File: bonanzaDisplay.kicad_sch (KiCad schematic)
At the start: 73 parts, among them J1 OLED-1.31-SSD1322, J15 SWD, J5 Conn_01x10, J6 USB_C_Receptacle_USB2.0, SW1 TS-1088-AR02016, SW2 TS-1088-AR02016, SW4 7*7*5-6P WX, U1 RP2354A, U10 TPS82130, U2 XC6206P302MR, U3 XC6206P282MR, Y1 ABM8-272-T3

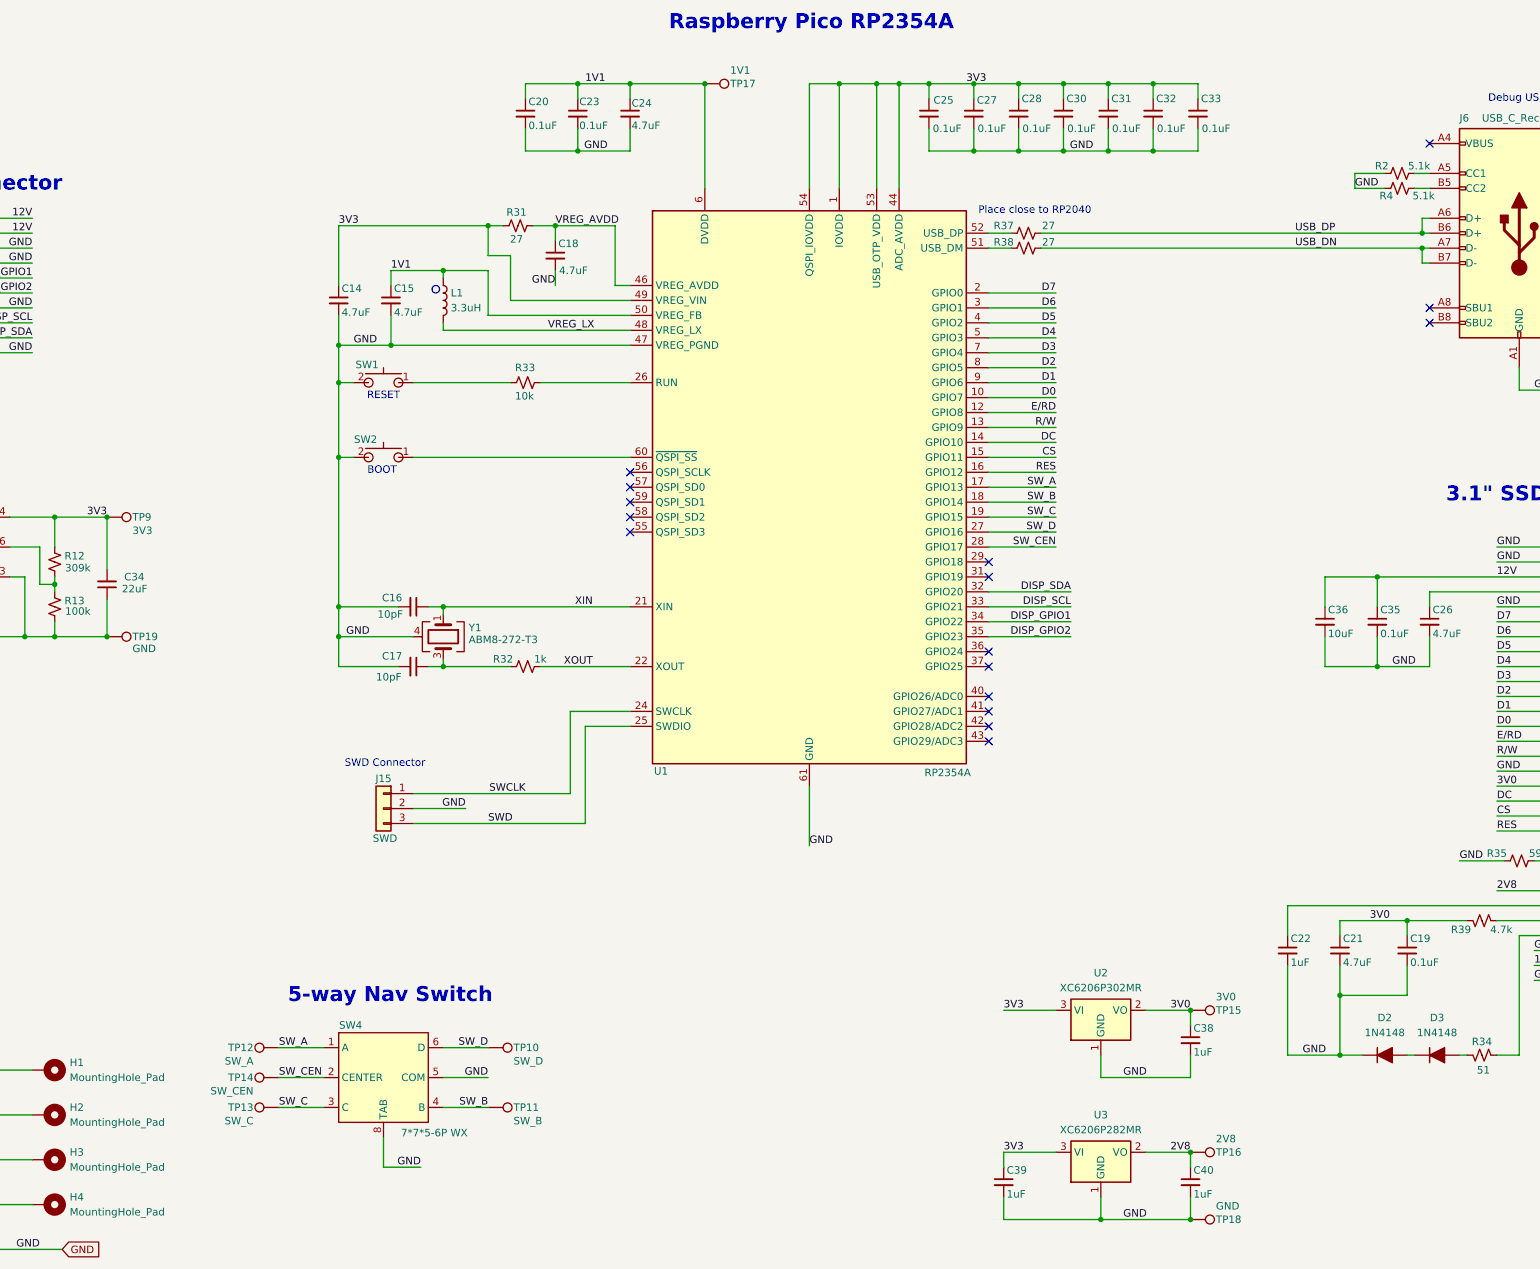
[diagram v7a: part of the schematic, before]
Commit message: updated LCSC part numbers
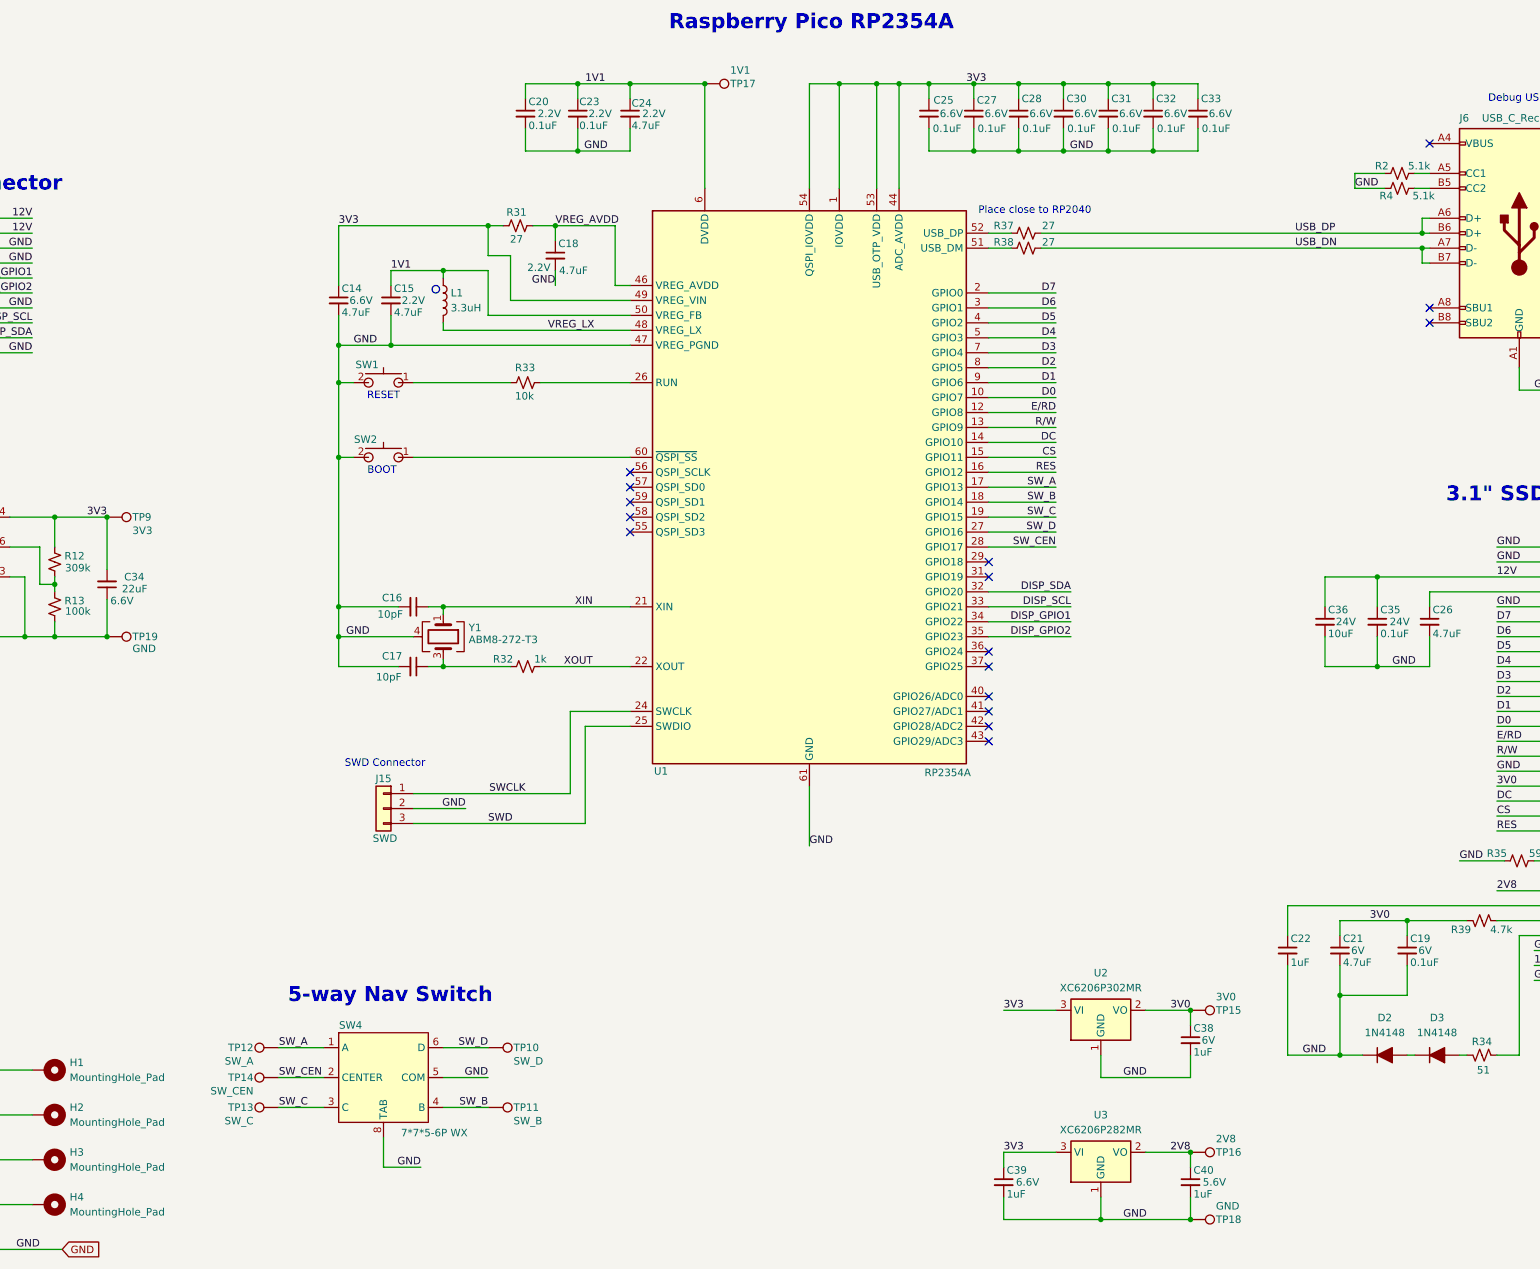
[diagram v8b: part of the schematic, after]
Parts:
- C14: LCSC (none) -> C368809; Voltage (none) -> 6.6V
- C15, C18, C24: LCSC (none) -> C368809; Voltage (none) -> 2.2V
- C16, C17: LCSC (none) -> C161512
- C19: LCSC (none) -> C77020; Voltage (none) -> 6V
- C20, C23: LCSC (none) -> C77020; Voltage (none) -> 2.2V
- C21: LCSC (none) -> C368809; Voltage (none) -> 6V
- C22: LCSC (none) -> C29266
- C25, C27, C28, C30, C31, C32, C33: LCSC (none) -> C77020; Voltage (none) -> 6.6V
- C26: LCSC (none) -> C368809
- C29: LCSC (none) -> C307337
- C34: LCSC (none) -> C386093; Voltage (none) -> 6.6V
- C35: LCSC (none) -> C77020; Voltage (none) -> 24V
- C36: LCSC (none) -> C15850; Voltage (none) -> 24V
- C38: LCSC (none) -> C29266; Voltage (none) -> 6V
- C39: LCSC (none) -> C29266; Voltage (none) -> 6.6V
- C40: LCSC (none) -> C29266; Voltage (none) -> 5.6V
- C8, TP14: LCSC (none) -> C344022
- D2, D3: LCSC (none) -> C917006
- J5: LCSC (none) -> C2908569
- J6: LCSC (none) -> C2988369
- R12, Y1: LCSC (none) -> C171694
- R13: LCSC (none) -> C60491
- R31, R37, R38, TP19: LCSC (none) -> C138021
- R32: LCSC (none) -> C106235
- R33: LCSC (none) -> C60490
- R34, R39: LCSC (none) -> C137960
- R35: LCSC (none) -> C477764
- U1: LCSC (none) -> C41378174
- U10: LCSC C473914 -> C106235
- U2: LCSC C347375 -> C477764
